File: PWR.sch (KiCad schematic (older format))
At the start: 20 parts, among them J601 PWR, U601 LM1117-3.3, U602 ADP7118

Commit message: libs added
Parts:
- U602: symbol user:ADP7118 -> ESP32-Eurorack-Audio-rescue:ADP7118-user
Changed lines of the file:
@@
 EESchema Schematic File Version 4
+LIBS:ESP32-Eurorack-Audio-cache
 EELAYER 29 0
 EELAYER END
@@
 VIN
 $Comp
-L user:ADP7118 U602
+L ESP32-Eurorack-Audio-rescue:ADP7118-user U602
 U 1 1 5B683013
 P 3550 4000
+AR Path="/5B683013" Ref="U602"  Part="1"
+AR Path="/5B69D53C/5B683013" Ref="U602"  Part="1"
 F 0 "U602" H 3925 4315 50  0000 C CNN
 F 1 "ADP7118" H 3925 4224 50  0000 C CNN

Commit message: current
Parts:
- removed U601: LM1117-3.3, Package_TO_SOT_SMD:TO-252-2, symbol Regulator_Linear:LM1117-3.3
- added C608: 1000u, Capacitor_SMD:CP_Elec_10x12.6, symbol Device:CP
- added R603: 10, Resistor_SMD:R_2512_6332Metric, symbol Device:R
- added TP601: 3V3D, TestPoint:TestPoint_Keystone_5019_Minature, symbol Connector:TestPoint
- added U601: R-78E3.3-1.0, Package_SIP:SIP3_11.6x8.5mm, symbol Regulator_Linear:L7805
- D604: footprint LED_SMD:LED_1206_3216Metric_Castellated -> LED_THT:LED_D5.0mm_Clear
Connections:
- net +3V3: now also TP601.1, U601.3 (OUT)
- net GND: now also C608.2, U601.2 (GND)
- net at C606.1, JP601.2 (C), U602.1 (VIN)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: now also R603.2
- new net: C608.1, R603.1, U601.1 (IN)
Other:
- note added: "1Watt!"
- note added: "ESR<=18mOhm!\n"
- moved on the sheet: C604, C605, D604, R602
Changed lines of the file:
@@
 Title "ESP32 Eurorack Audio Module"
 Date "2019-03-27"
-Rev "B2-public"
+Rev "C"
 Comp "(c) Robert Manzke 2019"
 Comment1 "https://creativecommons.org/licenses/by-nc-sa/4.0/"
@@
 Comment4 ""
 $EndDescr
-$Comp
-L Regulator_Linear:LM1117-3.3 U601
-U 1 1 5B69D584
-P 3700 2800
-F 0 "U601" H 3700 3042 50  0000 C CNN
-F 1 "LM1117-3.3" H 3700 2951 50  0000 C CNN
-F 2 "Package_TO_SOT_SMD:TO-252-2" H 3700 2800 50  0001 C CNN
-F 3 "http://www.ti.com/lit/ds/symlink/lm1117.pdf" H 3700 2800 50  0001 C CNN
-	1    3700 2800
-	1    0    0    -1
-$EndComp
 $Comp
 L Connector_Generic:Conn_02x05_Odd_Even J601
@@
 L power:GND #PWR0614
 U 1 1 5B69FCD6
-P 3700 3350
-F 0 "#PWR0614" H 3700 3100 50  0001 C CNN
-F 1 "GND" H 3705 3177 50  0000 C CNN
-F 2 "" H 3700 3350 50  0001 C CNN
-F 3 "" H 3700 3350 50  0001 C CNN
-	1    3700 3350
-	1    0    0    -1
-$EndComp
-Wire Wire Line
-	3700 3100 3700 3250
+P 4500 3350
+F 0 "#PWR0614" H 4500 3100 50  0001 C CNN
+F 1 "GND" H 4505 3177 50  0000 C CNN
+F 2 "" H 4500 3350 50  0001 C CNN
+F 3 "" H 4500 3350 50  0001 C CNN
+	1    4500 3350
+	1    0    0    -1
+$EndComp
+Wire Wire Line
+	4500 3100 4500 3250
 $Comp
 L power:+12V #PWR0612
@@
 L power:+3.3V #PWR0613
 U 1 1 5B6A0578
-P 4550 2650
-F 0 "#PWR0613" H 4550 2500 50  0001 C CNN
-F 1 "+3.3V" H 4565 2823 50  0000 C CNN
-F 2 "" H 4550 2650 50  0001 C CNN
-F 3 "" H 4550 2650 50  0001 C CNN
-	1    4550 2650
-	1    0    0    -1
-$EndComp
-Wire Wire Line
-	4000 2800 4150 2800
-Wire Wire Line
-	4550 2800 4550 2650
+P 5500 2650
+F 0 "#PWR0613" H 5500 2500 50  0001 C CNN
+F 1 "+3.3V" H 5515 2823 50  0000 C CNN
+F 2 "" H 5500 2650 50  0001 C CNN
+F 3 "" H 5500 2650 50  0001 C CNN
+	1    5500 2650
+	1    0    0    -1
+$EndComp
+Wire Wire Line
+	4800 2800 5100 2800
+Wire Wire Line
+	5500 2800 5500 2650
 $Comp
 L Device:CP C602
@@
 L Device:CP C604
 U 1 1 5B6A249E
-P 4150 3050
-F 0 "C604" H 4268 3096 50  0000 L CNN
-F 1 "22u" H 4268 3005 50  0000 L CNN
-F 2 "Capacitor_Tantalum_SMD:CP_EIA-3216-12_Kemet-S" H 4188 2900 50  0001 C CNN
-F 3 "~" H 4150 3050 50  0001 C CNN
-	1    4150 3050
-	1    0    0    -1
-$EndComp
-Wire Wire Line
-	4150 2800 4150 2900
-Connection ~ 4150 2800
-Wire Wire Line
-	4150 2800 4550 2800
-Wire Wire Line
-	4150 3200 4150 3250
-Wire Wire Line
-	4150 3250 3700 3250
-Connection ~ 3700 3250
-Wire Wire Line
-	3700 3250 3700 3350
+P 5100 3050
+F 0 "C604" H 5218 3096 50  0000 L CNN
+F 1 "22u" H 5218 3005 50  0000 L CNN
+F 2 "Capacitor_Tantalum_SMD:CP_EIA-3216-12_Kemet-S" H 5138 2900 50  0001 C CNN
+F 3 "~" H 5100 3050 50  0001 C CNN
+	1    5100 3050
+	1    0    0    -1
+$EndComp
+Wire Wire Line
+	5100 2800 5100 2900
+Connection ~ 5100 2800
+Wire Wire Line
+	5100 2800 5500 2800
+Wire Wire Line
+	5100 3200 5100 3250
+Wire Wire Line
+	5100 3250 4500 3250
+Connection ~ 4500 3250
+Wire Wire Line
+	4500 3250 4500 3350
 $Comp
 L Device:C C605
 U 1 1 5B6A31D3
-P 4550 3050
-F 0 "C605" H 4665 3096 50  0000 L CNN
-F 1 "100n" H 4665 3005 50  0000 L CNN
-F 2 "Capacitor_SMD:C_0603_1608Metric" H 4588 2900 50  0001 C CNN
-F 3 "~" H 4550 3050 50  0001 C CNN
-	1    4550 3050
-	1    0    0    -1
-$EndComp
-Wire Wire Line
-	4550 2800 4550 2900
-Connection ~ 4550 2800
-Wire Wire Line
-	4550 3200 4550 3250
-Wire Wire Line
-	4550 3250 4150 3250
-Connection ~ 4150 3250
+P 5500 3050
+F 0 "C605" H 5615 3096 50  0000 L CNN
+F 1 "100n" H 5615 3005 50  0000 L CNN
+F 2 "Capacitor_SMD:C_0603_1608Metric" H 5538 2900 50  0001 C CNN
+F 3 "~" H 5500 3050 50  0001 C CNN
+	1    5500 3050
+	1    0    0    -1
+$EndComp
+Wire Wire Line
+	5500 2800 5500 2900
+Connection ~ 5500 2800
+Wire Wire Line
+	5500 3200 5500 3250
+Wire Wire Line
+	5500 3250 5100 3250
+Connection ~ 5100 3250
 Wire Wire Line
 	4950 4000 4950 3850
@@
 L Device:LED D604
 U 1 1 5B6A709D
-P 5400 3000
-F 0 "D604" V 5438 2882 50  0000 R CNN
-F 1 "APTD3216SURCK" V 5347 2882 50  0000 R CNN
-F 2 "LED_SMD:LED_1206_3216Metric_Castellated" H 5400 3000 50  0001 C CNN
-F 3 "~" H 5400 3000 50  0001 C CNN
-	1    5400 3000
+P 6350 3000
+F 0 "D604" V 6388 2882 50  0000 R CNN
+F 1 "APTD3216SURCK" V 6297 2882 50  0000 R CNN
+F 2 "LED_THT:LED_D5.0mm_Clear" H 6350 3000 50  0001 C CNN
+F 3 "~" H 6350 3000 50  0001 C CNN
+	1    6350 3000
 	0    -1   -1   0
 $EndComp
@@
 L Device:R R602
 U 1 1 5B6A7164
-P 5050 2800
-F 0 "R602" V 4843 2800 50  0000 C CNN
-F 1 "68" V 4934 2800 50  0000 C CNN
-F 2 "Resistor_SMD:R_0805_2012Metric" V 4980 2800 50  0001 C CNN
-F 3 "~" H 5050 2800 50  0001 C CNN
-	1    5050 2800
+P 6000 2800
+F 0 "R602" V 5793 2800 50  0000 C CNN
+F 1 "68" V 5884 2800 50  0000 C CNN
+F 2 "Resistor_SMD:R_0805_2012Metric" V 5930 2800 50  0001 C CNN
+F 3 "~" H 6000 2800 50  0001 C CNN
+	1    6000 2800
 	0    1    1    0
 $EndComp
 Wire Wire Line
-	4550 2800 4900 2800
-Wire Wire Line
-	5200 2800 5400 2800
-Wire Wire Line
-	5400 2800 5400 2850
-Wire Wire Line
-	5400 3150 5400 3250
-Wire Wire Line
-	5400 3250 4550 3250
-Connection ~ 4550 3250
+	5500 2800 5850 2800
+Wire Wire Line
+	6150 2800 6350 2800
+Wire Wire Line
+	6350 2800 6350 2850
+Wire Wire Line
+	6350 3150 6350 3250
+Wire Wire Line
+	6350 3250 5500 3250
+Connection ~ 5500 3250
 $Comp
 L Jumper:Jumper_3_Bridged12 JP601
@@
 Wire Wire Line
 	9150 1650 8450 1650
+$Comp
+L Regulator_Linear:L7805 U601
+U 1 1 5CA2059B
+P 4500 2800
+F 0 "U601" H 4500 3042 50  0000 C CNN
+F 1 "R-78E3.3-1.0" H 4500 2951 50  0000 C CNN
+F 2 "Package_SIP:SIP3_11.6x8.5mm" H 4525 2650 50  0001 L CIN
+F 3 "http://www.st.com/content/ccc/resource/technical/document/datasheet/41/4f/b3/b0/12/d4/47/88/CD00000444.pdf/files/CD00000444.pdf/jcr:content/translations/en.CD00000444.pdf" H 4500 2750 50  0001 C CNN
+	1    4500 2800
+	1    0    0    -1
+$EndComp
+$Comp
+L Device:R R603
+U 1 1 5CA26F1C
+P 3550 2800
+F 0 "R603" V 3343 2800 50  0000 C CNN
+F 1 "10" V 3434 2800 50  0000 C CNN
+F 2 "Resistor_SMD:R_2512_6332Metric" V 3480 2800 50  0001 C CNN
+F 3 "~" H 3550 2800 50  0001 C CNN
+	1    3550 2800
+	0    1    1    0
+$EndComp
+$Comp
+L Device:CP C608
+U 1 1 5CA275D4
+P 3850 3050
+F 0 "C608" H 3968 3096 50  0000 L CNN
+F 1 "1000u" H 3968 3005 50  0000 L CNN
+F 2 "Capacitor_SMD:CP_Elec_10x12.6" H 3888 2900 50  0001 C CNN
+F 3 "~" H 3850 3050 50  0001 C CNN
+	1    3850 3050
+	1    0    0    -1
+$EndComp
+Wire Wire Line
+	3700 2800 3850 2800
+Wire Wire Line
+	3850 2800 3850 2900
+Wire Wire Line
+	4200 2800 3850 2800
+Connection ~ 3850 2800
+Wire Wire Line
+	4500 3250 3850 3250
+Wire Wire Line
+	3850 3250 3850 3200
+$Comp
+L power:PWR_FLAG #FLG0102
+U 1 1 5CA4E308
+P 3850 2700
+F 0 "#FLG0102" H 3850 2775 50  0001 C CNN
+F 1 "PWR_FLAG" H 3850 2873 50  0000 C CNN
+F 2 "" H 3850 2700 50  0001 C CNN
+F 3 "~" H 3850 2700 50  0001 C CNN
+	1    3850 2700
+	1    0    0    -1
+$EndComp
+Wire Wire Line
+	3850 2700 3850 2800
+Text Notes 3850 3200 0    50   ~ 0
+ESR<=18mOhm!\n
+Text Notes 3450 2950 0    50   ~ 0
+1Watt!
+$Comp
+L Connector:TestPoint TP601
+U 1 1 5CA30973
+P 5100 2650
+F 0 "TP601" H 5158 2768 50  0000 L CNN
+F 1 "3V3D" H 5158 2677 50  0000 L CNN
+F 2 "TestPoint:TestPoint_Keystone_5019_Minature" H 5300 2650 50  0001 C CNN
+F 3 "~" H 5300 2650 50  0001 C CNN
+	1    5100 2650
+	1    0    0    -1
+$EndComp
+Wire Wire Line
+	5100 2650 5100 2800
 $EndSCHEMATC

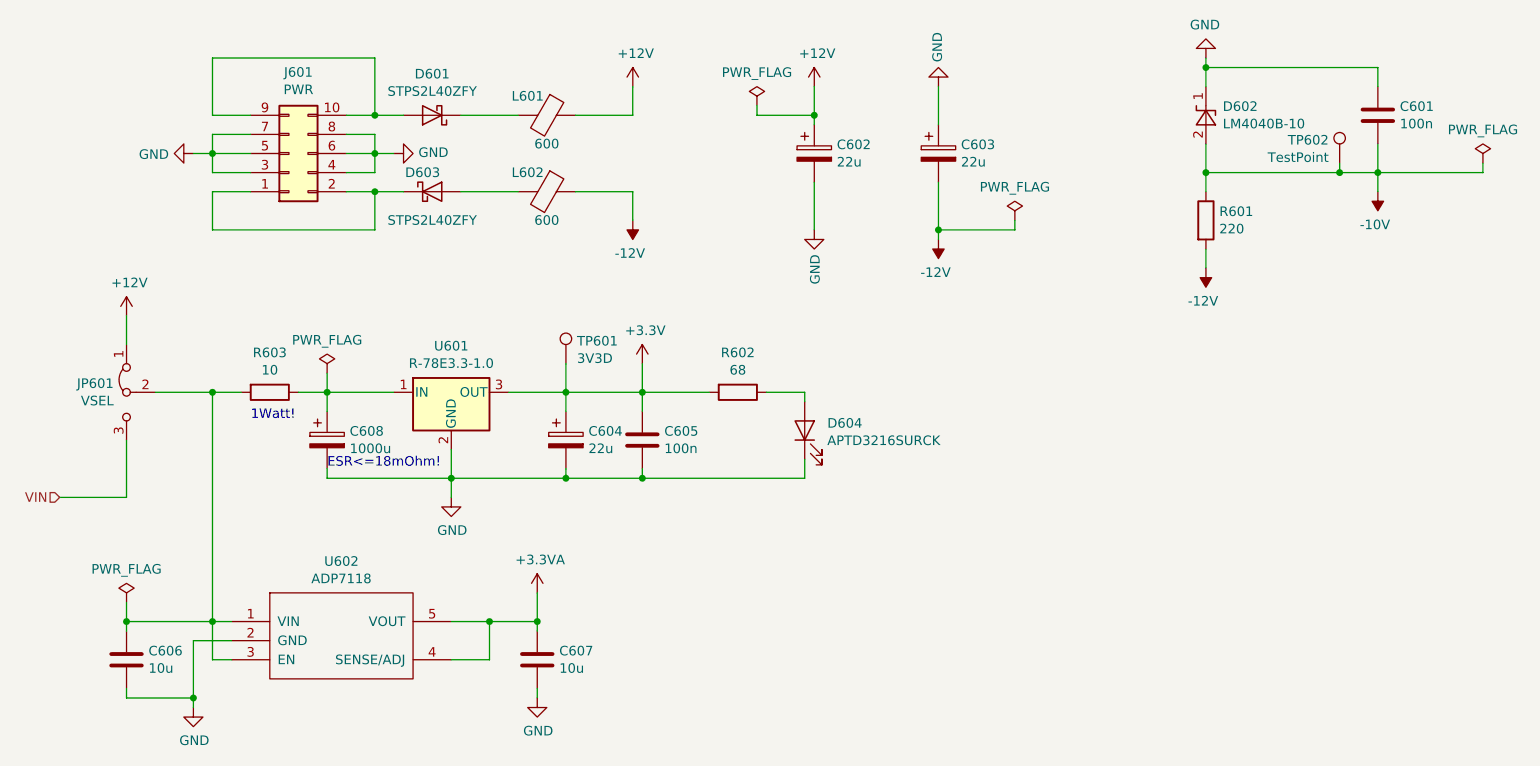
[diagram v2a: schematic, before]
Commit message: cleaned up schematic
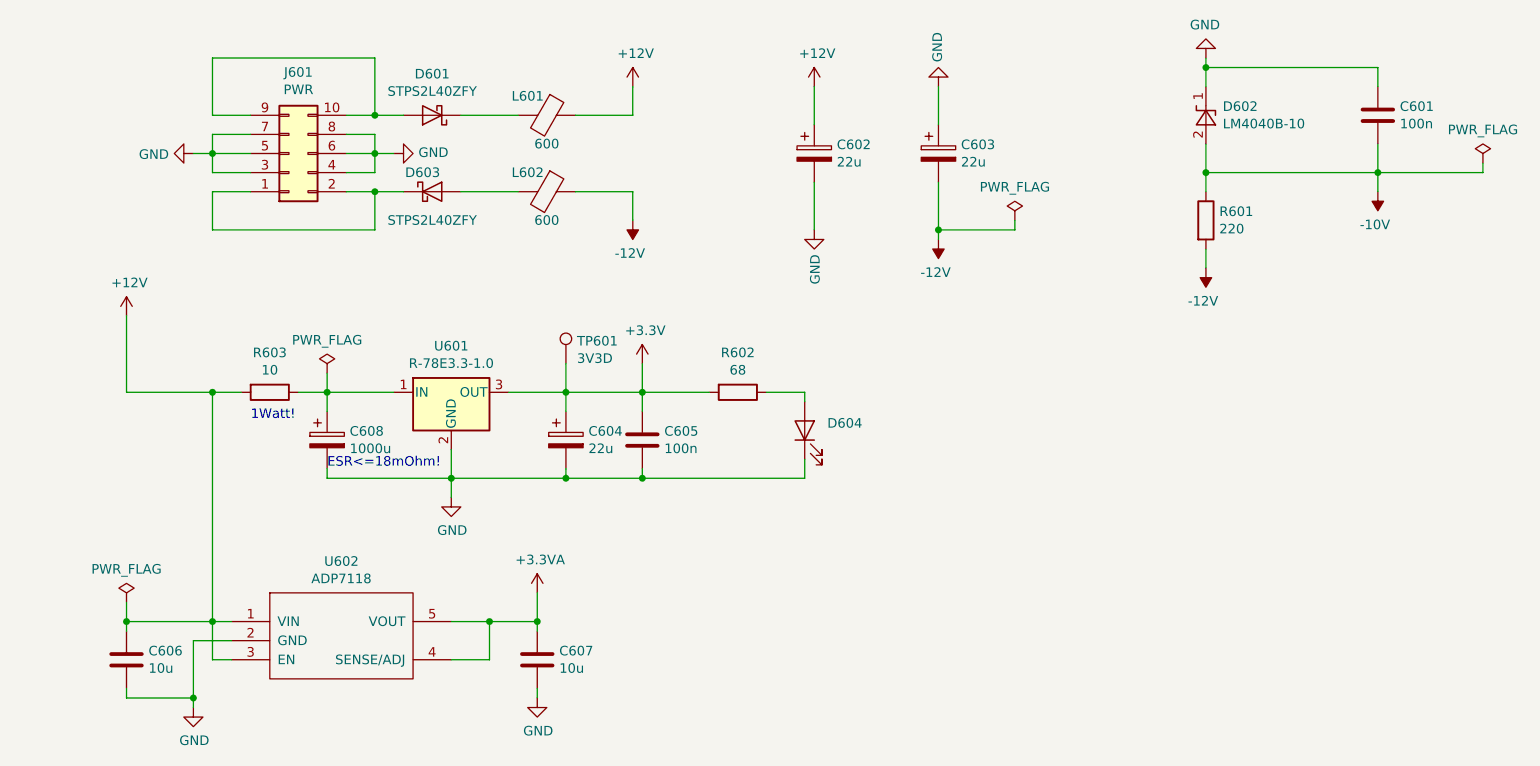
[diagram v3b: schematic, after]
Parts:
- removed JP601: VSEL, Connector_PinHeader_2.54mm:PinHeader_1x03_P2.54mm_Vertical, symbol Jumper:Jumper_3_Bridged12
- removed TP602: TestPoint, TestPoint:TestPoint_Keystone_5019_Minature, symbol Connector:TestPoint
- D604: value APTD3216SURCK -> ~
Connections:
- net +12V: now also C606.1, R603.2, U602.1 (VIN), U602.3 (EN)
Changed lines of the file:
@@
 Sheet 6 8
 Title "ESP32 Eurorack Audio Module"
-Date "2019-03-27"
-Rev "C"
+Date "2019-05-13"
+Rev "D"
 Comp "(c) Robert Manzke 2019"
 Comment1 "https://creativecommons.org/licenses/by-nc-sa/4.0/"
@@
 	1    0    0    -1
 $EndComp
-Wire Wire Line
-	2800 2400 2800 2550
 $Comp
 L power:+3.3V #PWR0613
@@
 	1    0    0    -1
 $EndComp
-Wire Wire Line
-	6400 1200 6400 1350
 $Comp
 L power:GND #PWR0609
@@
 P 6350 3000
 F 0 "D604" V 6388 2882 50  0000 R CNN
-F 1 "APTD3216SURCK" V 6297 2882 50  0000 R CNN
+F 1 "~" V 6297 2882 50  0000 R CNN
 F 2 "LED_THT:LED_D5.0mm_Clear" H 6350 3000 50  0001 C CNN
 F 3 "~" H 6350 3000 50  0001 C CNN
@@
 	6350 3250 5500 3250
 Connection ~ 5500 3250
-$Comp
-L Jumper:Jumper_3_Bridged12 JP601
-U 1 1 5B6ADE26
-P 2800 2800
-F 0 "JP601" V 2754 2867 50  0000 L CNN
-F 1 "VSEL" V 2845 2867 50  0000 L CNN
-F 2 "Connector_PinHeader_2.54mm:PinHeader_1x03_P2.54mm_Vertical" H 2800 2800 50  0001 C CNN
-F 3 "~" H 2800 2800 50  0001 C CNN
-	1    2800 2800
-	0    -1   1    0
-$EndComp
 Wire Wire Line
 	3250 2800 3250 4000
-Wire Wire Line
-	2950 2800 3250 2800
 Connection ~ 3250 2800
 Wire Wire Line
 	3250 2800 3400 2800
-Wire Wire Line
-	2800 3050 2800 3350
-Wire Wire Line
-	2800 3350 2450 3350
-Text HLabel 2450 3350 0    50   Input ~ 0
-VIN
 $Comp
 L ESP32-Eurorack-Audio-rescue:ADP7118-user U602
@@
 	7050 1950 7050 2000
 $Comp
-L power:PWR_FLAG #FLG0601
-U 1 1 5B9057C9
-P 6100 1300
-F 0 "#FLG0601" H 6100 1375 50  0001 C CNN
-F 1 "PWR_FLAG" H 6100 1474 50  0000 C CNN
-F 2 "" H 6100 1300 50  0001 C CNN
-F 3 "~" H 6100 1300 50  0001 C CNN
-	1    6100 1300
-	1    0    0    -1
-$EndComp
-Wire Wire Line
-	6400 1350 6100 1350
-Wire Wire Line
-	6100 1350 6100 1300
-Connection ~ 6400 1350
-Wire Wire Line
-	6400 1350 6400 1400
-$Comp
 L Device:R R601
 U 1 1 5B91EBF6
@@
 Wire Wire Line
 	9350 1500 9350 1650
-Wire Wire Line
-	9350 1650 9150 1650
 Connection ~ 8450 1650
 Wire Wire Line
@@
 	9900 1650 9900 1600
 $Comp
-L Connector:TestPoint TP602
-U 1 1 5B6D7C4D
-P 9150 1600
-F 0 "TP602" H 9093 1720 50  0000 R CNN
-F 1 "TestPoint" H 9093 1629 50  0000 R CNN
-F 2 "TestPoint:TestPoint_Keystone_5019_Minature" H 9350 1600 50  0001 C CNN
-F 3 "~" H 9350 1600 50  0001 C CNN
-	1    9150 1600
-	1    0    0    -1
-$EndComp
-Wire Wire Line
-	9150 1600 9150 1650
-Connection ~ 9150 1650
-Wire Wire Line
-	9150 1650 8450 1650
-$Comp
 L Regulator_Linear:L7805 U601
 U 1 1 5CA2059B
@@
 Wire Wire Line
 	5100 2650 5100 2800
+Wire Wire Line
+	8450 1650 9350 1650
+Wire Wire Line
+	2800 2800 2800 2400
+Wire Wire Line
+	2800 2800 3250 2800
+Wire Wire Line
+	6400 1200 6400 1400
 $EndSCHEMATC

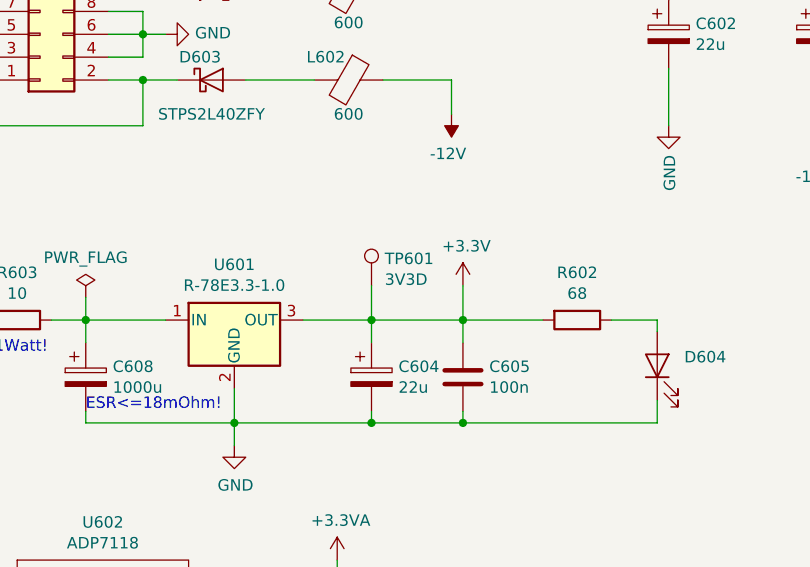
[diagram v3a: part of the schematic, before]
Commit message: added pcb fiducials, updated date
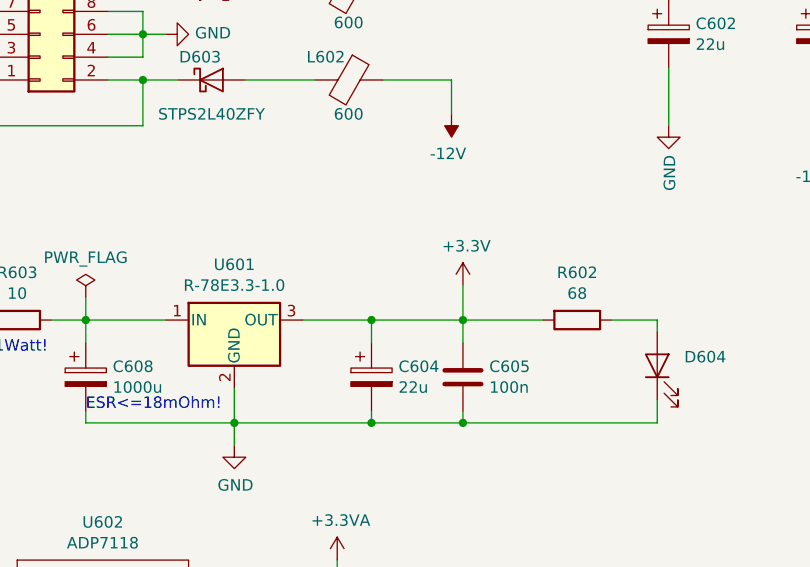
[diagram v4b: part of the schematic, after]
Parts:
- removed TP601: 3V3D, TestPoint:TestPoint_Keystone_5019_Minature, symbol Connector:TestPoint
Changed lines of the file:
@@
 Sheet 6 8
 Title "ESP32 Eurorack Audio Module"
-Date "2019-05-13"
+Date "2019-06-13"
 Rev "D"
 Comp "(c) Robert Manzke 2019"
@@
 Text Notes 3450 2950 0    50   ~ 0
 1Watt!
-$Comp
-L Connector:TestPoint TP601
-U 1 1 5CA30973
-P 5100 2650
-F 0 "TP601" H 5158 2768 50  0000 L CNN
-F 1 "3V3D" H 5158 2677 50  0000 L CNN
-F 2 "TestPoint:TestPoint_Keystone_5019_Minature" H 5300 2650 50  0001 C CNN
-F 3 "~" H 5300 2650 50  0001 C CNN
-	1    5100 2650
-	1    0    0    -1
-$EndComp
-Wire Wire Line
-	5100 2650 5100 2800
 Wire Wire Line
 	8450 1650 9350 1650
